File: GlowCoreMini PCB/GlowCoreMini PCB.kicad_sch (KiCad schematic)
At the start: 63 parts, among them P1 Solder_Pad, P10 Solder_Pad, P11 Solder_Pad, P12 Solder_Pad, P13 Solder_Pad, P14 Solder_Pad, P2 Solder_Pad, P3 Solder_Pad, P4 Solder_Pad, P5 Solder_Pad, P6 Solder_Pad, P7 Solder_Pad, P8 Solder_Pad, P9 Solder_Pad, SW1 TS24CA, SW2 TS24CA, SW3 TS24CA, SW4 TS24CA, U1 ESP32-WROOM-32E, U11 AO3400A, U12 CP2102-GMR, U14 UMH3N, U2 SN74LVC2T45DCUR, U3 MSM261D4030H1CPM, U4 SN74LVC1G373DBVR, U5 AP40P05, U6 SPX3819M5-L-3-3_TR, U7 SS54, U8 SK9822-EC20, U9 SN74LVC1G373DBVR

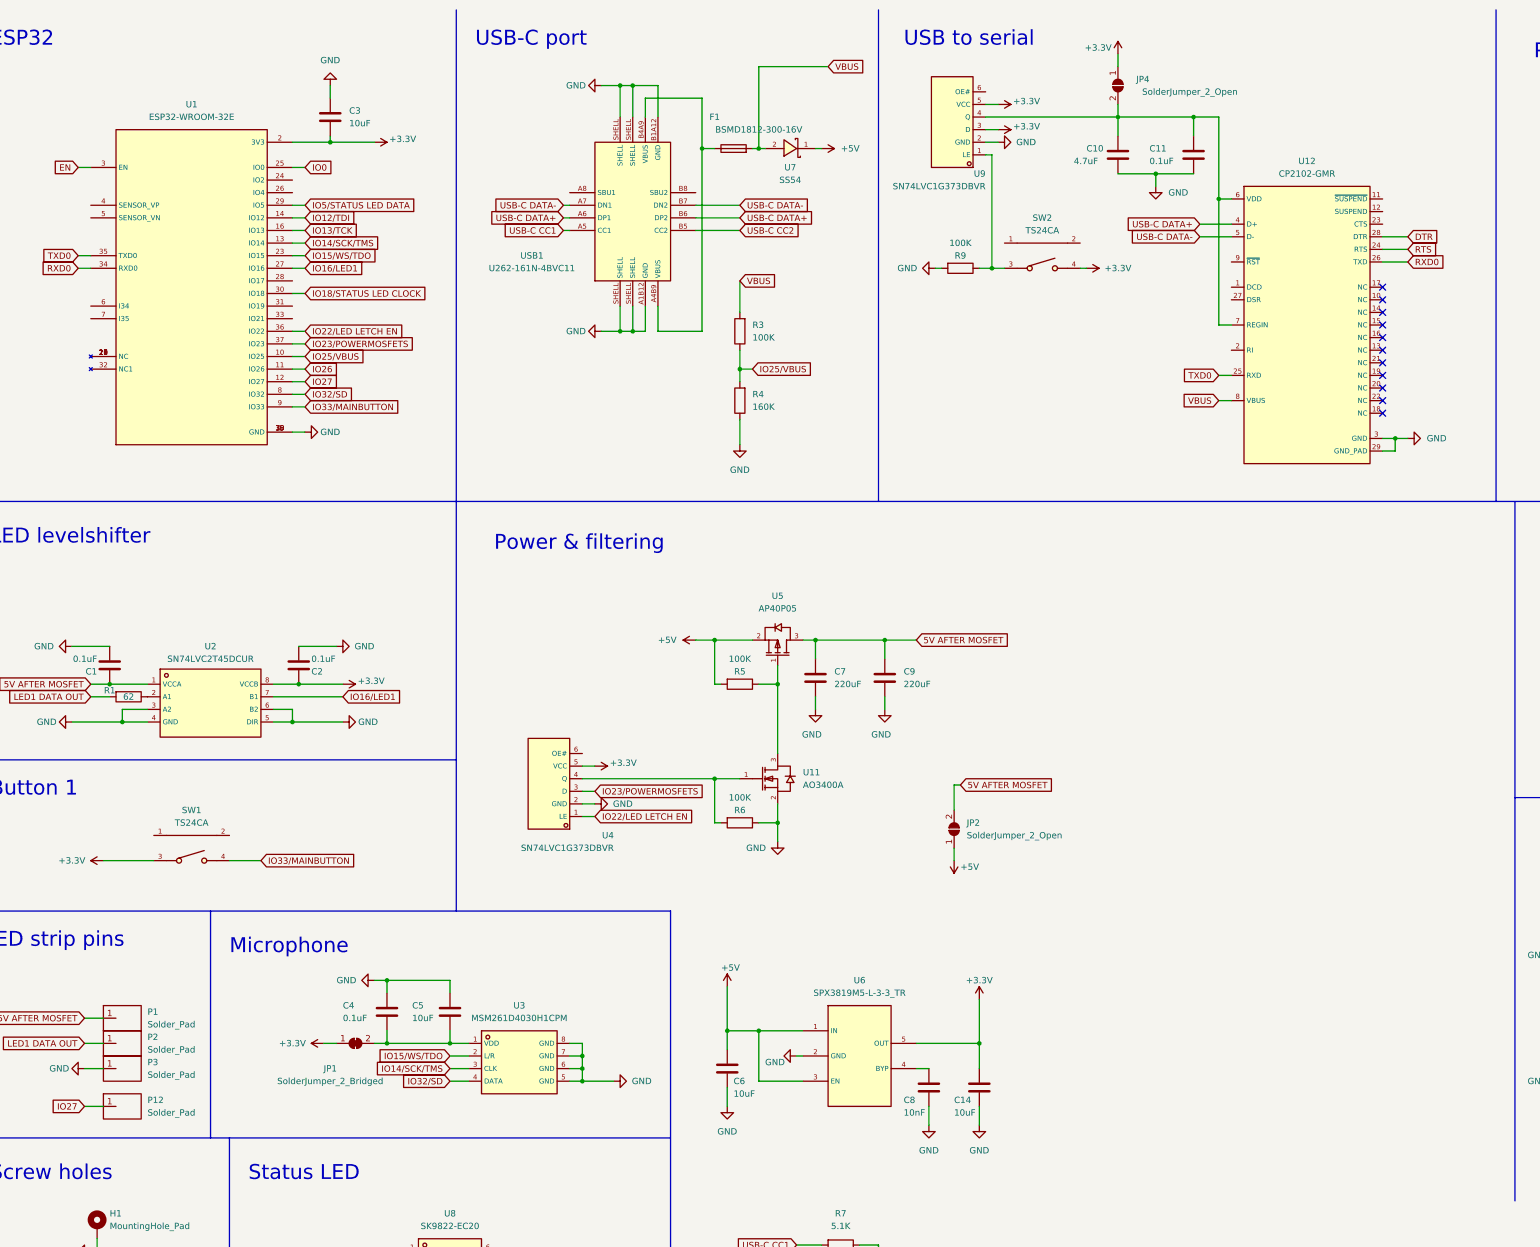
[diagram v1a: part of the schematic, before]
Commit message: updated 3D printed case design
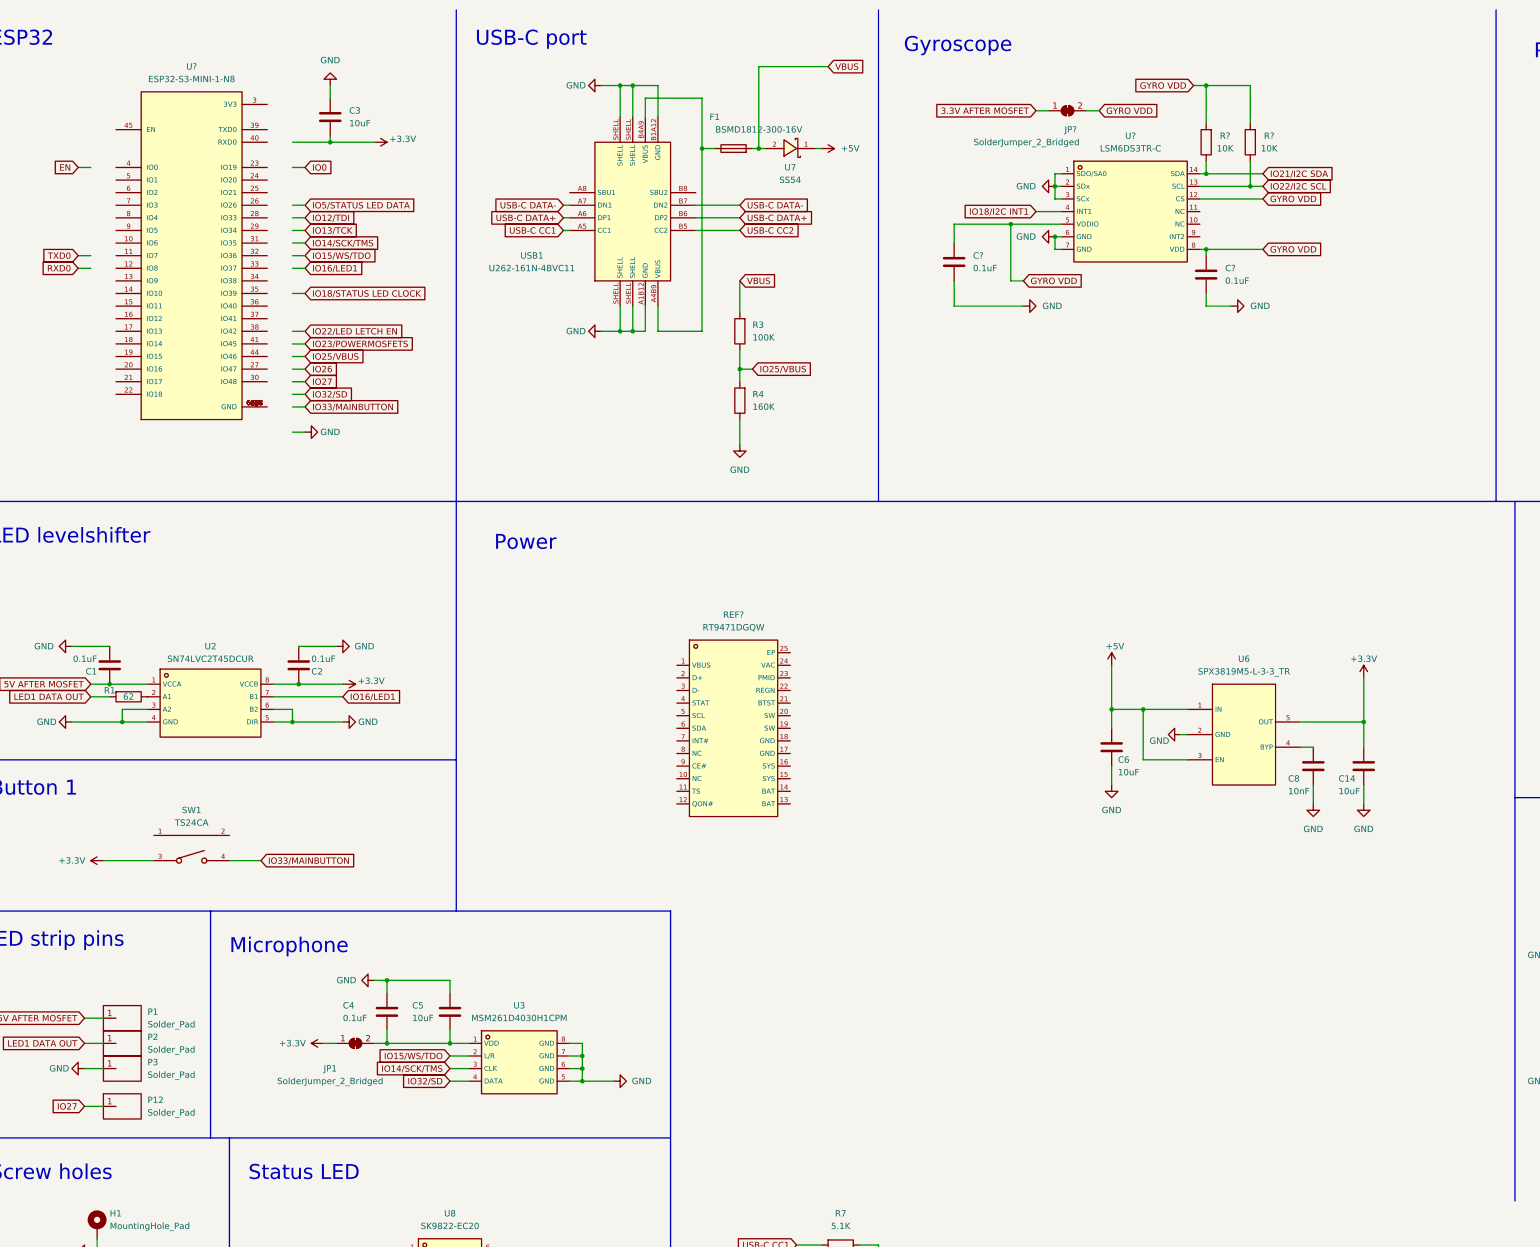
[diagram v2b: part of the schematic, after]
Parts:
- removed C10: 4.7uF, Capacitor_SMD:C_0603_1608Metric, symbol Device:C
- removed C11: 0.1uF, Capacitor_SMD:C_0402_1005Metric, symbol Device:C
- removed C7, C9: 220uF, Capacitor_SMD:C_1206_3216Metric_Pad1.33x1.80mm_HandSolder, symbol Device:C
- removed JP2, JP4: SolderJumper_2_Open, Jumper:SolderJumper-2_P1.3mm_Open_RoundedPad1.0x1.5mm, symbol Jumper:SolderJumper_2_Open
- removed R5, R6, R9: 100K, Resistor_SMD:R_0402_1005Metric, symbol Device:10K 0603
- removed SW2: TS24CA, footprint:SW-SMD_TS24CA, symbol MyParts:TS24CA
- removed U1: ESP32-WROOM-32E, footprint:WIFI-SMD_ESP32-WROOM-32E, symbol MyParts:ESP32-WROOM-32E
- removed U11: AO3400A, footprint:SOT-23-3_L2.9-W1.6-P1.90-LS2.8-BR, symbol MyParts:AO3400A
- removed U12: CP2102-GMR, footprint:QFN-28_L5.0-W5.0-P0.50-BL-EP, symbol MyParts:CP2102-GMR
- removed U4, U9: SN74LVC1G373DBVR, footprint:SOT-23-6_L2.9-W1.6-P0.95-LS2.8-BR, symbol MyParts:SN74LVC1G373DBVR
- removed U5: AP40P05, footprint:SOT-23-3_L2.9-W1.3-P1.90-LS2.4-BR, symbol MyParts:AP40P05
- added C? (x2): 0.1uF, Capacitor_SMD:C_0402_1005Metric, symbol Device:C
- added JP?: SolderJumper_2_Bridged, Jumper:SolderJumper-2_P1.3mm_Bridged_RoundedPad1.0x1.5mm, symbol Jumper:SolderJumper_2_Bridged
- added R? (x2): 10K, Resistor_SMD:R_0402_1005Metric, symbol Device:10K 0603
- added REF?: RT9471DGQW, footprint:WQFN-24_L4.0-W4.0-P0.50-TL-EP2.5, symbol MyParts:RT9471DGQW
- added U?: ESP32-S3-MINI-1-N8, footprint:ESP32-S3-MINI-1-N8, symbol MyParts:ESP32-S3-MINI-1-N8
- added U?: LSM6DS3TR-C, footprint:LGA-14_L3.0-W2.5-P0.50-TL, symbol MyParts:LSM6DS3TR-C
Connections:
- net GND: now also C?.2, C?.2, U?.1 (SDO/SA0), U?.2 (SDx), U?.3 (SCx), U?.6 (GND), U?.7 (GND)
- new net: U?.1 (GND), U?.2 (GND), U?.42 (GND), U?.43 (GND), U?.46 (GND), U?.47 (GND), U?.48 (GND), U?.49 (GND), U?.50 (GND), U?.51 (GND), U?.52 (GND), U?.53 (GND), U?.54 (GND), U?.55 (GND), U?.56 (GND), U?.57 (GND), U?.58 (GND), U?.59 (GND), U?.60 (GND), U?.61 (GND), U?.61_1 (GND), U?.61_2 (GND), U?.61_3 (GND), U?.61_4 (GND), U?.61_5 (GND), U?.61_6 (GND), U?.61_7 (GND), U?.61_8 (GND), U?.62 (GND), U?.63 (GND), U?.64 (GND), U?.65 (GND)
- new net 3.3V AFTER MOSFET: JP?.1 (A)
- new net GYRO VDD: C?.1, C?.1, JP?.2 (B), R?.2, R?.2, U?.12 (CS), U?.5 (VDDIO), U?.8 (VDD)
- new net IO18/I2C INT1: U?.4 (INT1)
- new net IO21/I2C SDA: R?.1, U?.14 (SDA)
- new net IO22/I2C SCL: R?.1, U?.13 (SCL)
- no-connect marks 11 -> 0
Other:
- note added: "Gyroscope"
- note added: "Power"
- note removed: "Power & filtering"
- note removed: "USB to serial"
- moved on the sheet: C14, C6, C8, U6

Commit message: continued redesign of pcb
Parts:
- removed C1, C2, C4, C? (x2): 0.1uF, Capacitor_SMD:C_0402_1005Metric, symbol Device:C
- removed C12, C14, C3, C6: 10uF, Capacitor_SMD:C_0603_1608Metric, symbol Device:10uF 0603
- removed C13: 1uF, Capacitor_SMD:C_0402_1005Metric, symbol Device:10uF 0603
- removed C5: 10uF, Capacitor_SMD:C_0603_1608Metric, symbol Device:0.1uF 0603
- removed C8: 10nF, Capacitor_SMD:C_0402_1005Metric, symbol Device:10uF 0603
- removed F1: BSMD1812-300-16V, Fuse:Fuse_1812_4532Metric_Pad1.30x3.40mm_HandSolder, symbol Device:Fuse
- removed H1, H2: MountingHole_Pad, MountingHole:MountingHole_2.2mm_M2_ISO7380, symbol Mechanical:MountingHole_Pad
- removed JP1, JP?: SolderJumper_2_Bridged, Jumper:SolderJumper-2_P1.3mm_Bridged_RoundedPad1.0x1.5mm, symbol Jumper:SolderJumper_2_Bridged
- removed P1, P10, P11, P12, P13, P14, P2, P3, P4, P5, P6, P7, P8, P9: Solder_Pad, footprint:Solder pad, symbol MyParts:Solder_Pad
- removed R1: 62, Resistor_SMD:R_0402_1005Metric, symbol Device:R
- removed R12, R13: 220, Resistor_SMD:R_0402_1005Metric, symbol Device:10K 0603
- removed R14, R15, R? (x2): 10K, Resistor_SMD:R_0402_1005Metric, symbol Device:10K 0603
- removed R3: 100K, Resistor_SMD:R_0402_1005Metric, symbol Device:R
- removed R4: 160K, Resistor_SMD:R_0603_1608Metric, symbol Device:R
- removed R7, R8: 5.1K, Resistor_SMD:R_0402_1005Metric, symbol Device:5.1K 1% 0603
- removed REF?: RT9471DGQW, footprint:WQFN-24_L4.0-W4.0-P0.50-TL-EP2.5, symbol MyParts:RT9471DGQW
- removed SW1, SW3, SW4: TS24CA, footprint:SW-SMD_TS24CA, symbol MyParts:TS24CA
- removed U14: UMH3N, footprint:SC-70-6_L2.2-W1.3-P0.65-LS2.1-BR, symbol LCSC:UMH3N
- removed U2: SN74LVC2T45DCUR, footprint:VSSOP-8_L2.4-W2.1-P0.50-LS3.2-BR, symbol MyParts:SN74LVC2T45DCUR
- removed U3: MSM261D4030H1CPM, footprint:MIC-SMD_8P-L3.0-W4.0-P0.85-BL, symbol MyParts:MSM261D4030H1CPM
- removed U6: SPX3819M5-L-3-3_TR, footprint:SOT-23-5_L3.0-W1.7-P0.95-LS2.8-BR, symbol MyParts:SPX3819M5-L-3-3_TR
- removed U7: SS54, footprint:SMA_L4.4-W2.8-LS5.4-RD, symbol MyParts:SS54
- removed U8: SK9822-EC20, footprint:LED-SMD_6P-L2.0-W2.0-P0.80-TL, symbol MyParts:SK9822-EC20
- removed U?: ESP32-S3-MINI-1-N8, footprint:ESP32-S3-MINI-1-N8, symbol MyParts:ESP32-S3-MINI-1-N8
- removed U?: LSM6DS3TR-C, footprint:LGA-14_L3.0-W2.5-P0.50-TL, symbol MyParts:LSM6DS3TR-C
- removed USB1: U262-161N-4BVC11, footprint:USB-3.1-SMD_U262-161N-4BVC11, symbol MyParts:U262-161N-4BVC11
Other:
- added sheet 3.3V converter (3_3_converter.kicad_sch)
- added sheet Battery (battery.kicad_sch)
- added sheet Battery Management IC (GlowCoreMini_BattIC.kicad_sch)
- added sheet Buttons (buttons.kicad_sch)
- added sheet ESP32 (GlowCoreMini_ESP32.kicad_sch)
- added sheet Gyroscope (gyroscope.kicad_sch)
- added sheet LED power (GlowCoreMini_LEDpower.kicad_sch)
- added sheet LED strips (ledstrips.kicad_sch)
- added sheet Microphone (microphone.kicad_sch)
- added sheet Pads (pads.kicad_sch)
- added sheet Status LED (statusled.kicad_sch)
- added sheet USB-C (GlowCoreMini_USBC.kicad_sch)
- note added: "3.3V converter"
- note added: "Battery"
- note added: "Battery IC"
- note added: "Buttons"
- note added: "GlowCore Mini"
- note added: "LED Power"
- note added: "LED strips"
- note added: "USB-C"
- note added: "v3.1"
- note removed: "Auto program DTR RTS --> EN IO0 1 1 1 1 0 0 1 1 1 0 0 1 0 1 1 0"
- note removed: "Autoreset"
- note removed: "Button 1"
- note removed: "LED levelshifter"
- note removed: "LED strip pins"
- note removed: "Power"
- note removed: "Reset"
- note removed: "Screw holes"
- note removed: "USB-C port"

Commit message: updated pcb design
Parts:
- added C1, C12: 1uF, Capacitor_SMD:C_0402_1005Metric, symbol Device:10uF 0603
- added C10, C11, C14, C16: 0.1uF, Capacitor_SMD:C_0402_1005Metric, symbol Device:C
- added C13: 0.1uF, Capacitor_SMD:C_0402_1005Metric, symbol Device:0.1uF 0603
- added C15: 10uF, Capacitor_SMD:C_0603_1608Metric, symbol Device:0.1uF 0603
- added C17, C19, C2, C3, C7, C8, C9: 10uF, Capacitor_SMD:C_0603_1608Metric, symbol Device:10uF 0603
- added C18: 10nF, Capacitor_SMD:C_0402_1005Metric, symbol Device:10uF 0603
- added C4: 220uF, Capacitor_SMD:C_1206_3216Metric, symbol Device:C
- added C5: 4.7uF, Capacitor_SMD:C_0402_1005Metric, symbol Device:10uF 0603
- added C6: 47nF, Capacitor_SMD:C_0402_1005Metric, symbol Device:10uF 0603
- added F1: BSMD1812-300-16V, Fuse:Fuse_1812_4532Metric_Pad1.30x3.40mm_HandSolder, symbol Device:Fuse
- added JP1: SolderJumper_2_Open, Jumper:SolderJumper-2_P1.3mm_Open_RoundedPad1.0x1.5mm, symbol Jumper:SolderJumper_2_Open
- added JP2: SolderJumper_2_Bridged, Jumper:SolderJumper-2_P1.3mm_Bridged_RoundedPad1.0x1.5mm, symbol Jumper:SolderJumper_2_Bridged
- added L1: WPN4020H1R0MT, footprint:IND-SMD_L4.0-W4.0_SLW40XX, symbol MyParts:WPN4020H1R0MT
- added P1, P10, P11, P12, P13, P14, P15, P16, P17, P18, P19, P2, P20, P21, P22, P3, P4, P5, P6, P7, P8, P9: Solder_Pad, footprint:Solder pad, symbol MyParts:Solder_Pad
- added R1, R13, R16, R19, R3, R9: 100K, Resistor_SMD:R_0402_1005Metric, symbol Device:R
- added R10, R11, R2, R20, R7, R8: 10K, Resistor_SMD:R_0402_1005Metric, symbol Device:10K 0603
- added R12, R21, R22, R5, R6: 100K, Resistor_SMD:R_0402_1005Metric, symbol Device:10K 0603
- added R14, R15: 62, Resistor_SMD:R_0402_1005Metric, symbol Device:R
- added R17, R23, R24: 5.1K, Resistor_SMD:R_0402_1005Metric, symbol Device:5.1K 1% 0603
- added R18: 33K, Resistor_SMD:R_0402_1005Metric, symbol Device:R
- added R4: 160K, Resistor_SMD:R_0603_1608Metric, symbol Device:R
- added REF1: RT9471DGQW, footprint:RT9471_vias_in_pad, symbol MyParts:RT9471DGQW
- added SW1, SW2, SW3: TS24CA, footprint:SW-SMD_TS24CA, symbol MyParts:TS24CA
- added U1: SN74LVC1G373DBVR, footprint:SOT-23-6_L2.9-W1.6-P0.95-LS2.8-BR, symbol MyParts:SN74LVC1G373DBVR
- added U10: LSM6DS3TR-C, footprint:LGA-14_L3.0-W2.5-P0.50-TL, symbol MyParts:LSM6DS3TR-C
- added U11: MSM261D4030H1CPM, footprint:MIC-SMD_8P-L4.0-W3.0_ZTS6231, symbol MyParts:MSM261D4030H1CPM
- added U12: SPX3819M5-L-3-3_TR, footprint:SOT-23-5_L3.0-W1.7-P0.95-LS2.8-BR, symbol MyParts:SPX3819M5-L-3-3_TR
- added U13: SK9822-EC20, footprint:LED-SMD_6P-L2.0-W2.0-P0.80-TL, symbol MyParts:SK9822-EC20
- added U14, U15, U4, U5, U8: AP40P05, footprint:SOT-23-3_L2.9-W1.3-P1.90-LS2.4-BR, symbol MyParts:AP40P05
- added U2: ESP32-S3-MINI-1-N8, footprint:ESP32-S3-MINI-1-N8, symbol MyParts:ESP32-S3-MINI-1-N8
- added U3: PTVSHC3N12VU, footprint:DFN-3_L2.0-W2.0-P1.30-BR, symbol MyParts:PTVSHC3N12VU
- added U6: AO3400A, footprint:SOT-23-3_L2.9-W1.6-P1.90-LS2.8-BR, symbol MyParts:AO3400A
- added U7: 74LVC2G04DW-7, footprint:SOT-363_L2.0-W1.3-P0.65-LS2.1-BR, symbol MyParts:74LVC2G04DW-7
- added U9: SN74LVC2T45DCUR, footprint:VSSOP-8_L2.4-W2.1-P0.50-LS3.2-BR, symbol MyParts:SN74LVC2T45DCUR
- added USB1: U262-161N-4BVC11, footprint:USB-3.1-SMD_U262-161N-4BVC11, symbol MyParts:U262-161N-4BVC11
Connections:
- new net: R15.1, U9.3 (A2)
- new net: C6.1, REF1.21 (BTST)
- new net: C6.2, L1.1, REF1.19 (SW), REF1.20 (SW)
- new net: R12.1, R21.1, R22.2, R5.1, U14.1 (G), U15.1 (G), U4.1 (G), U5.1 (G), U6.3 (D)
- new net: R10.2, R11.2, REF1.11 (TS)
- new net: C8.2, C9.2, JP2.1 (A), L1.2, REF1.15 (SYS), REF1.16 (SYS)
- new net: C2.2, REF1.23 (PMID)
- new net: P1.1, U8.3 (D)
- new net: C18.2, U12.4 (BYP)
- new net: R14.1, U9.2 (A1)
- new net: R6.2, U1.4 (Q), U6.1 (G)
- new net: R9.1, SW1.4, U7.1 (1A)
- new net: F1.1, JP1.1 (A), USB1.A4B9 (VBUS), USB1.B4A9 (VBUS)
- new net: R13.2, U8.1 (G)
- new net +3V3: C19.2, C3.2, P20.1, R12.2, R16.1, R17.1, R2.1, R20.1, R7.1, R8.1, R9.2, U1.5 (VCC), U12.5 (OUT), U15.2 (S), U2.3 (3V3), U7.5 (VCC)
- new net +BATT: C7.2, R18.2, REF1.13 (BAT), REF1.14 (BAT), U8.2 (S)
- new net -BATT: C1.1, C10.2, C11.2, C12.1, C13.1, C14.2, C15.1, C16.2, C17.1, C18.1, C19.1, C2.1, C3.1, C4.2, C5.2, C7.1, C8.1, C9.1, P15.1, P18.1, P2.1, P5.1, R1.2, R11.1, R13.1, R19.1, R23.1, R24.1, R4.1, R6.1, REF1.17 (GND), REF1.18 (GND), REF1.25 (EP), SW1.3, SW2.3, SW3.3, U1.2 (GND), U10.1 (SDO/SA0), U10.2 (SDx), U10.3 (SCx), U10.6 (GND), U10.7 (GND), U11.5 (GND), U11.6 (GND), U11.7 (GND), U11.8 (GND), U12.2 (GND), U13.2 (GND), U2.1 (GND), U2.2 (GND), U2.42 (GND), U2.43 (GND), U2.46 (GND), U2.47 (GND), U2.48 (GND), U2.49 (GND), U2.50 (GND), U2.51 (GND), U2.52 (GND), U2.53 (GND), U2.54 (GND), U2.55 (GND), U2.56 (GND), U2.57 (GND), U2.58 (GND), U2.59 (GND), U2.60 (GND), U2.61 (GND), U2.61_1 (GND), U2.61_2 (GND), U2.61_3 (GND), U2.61_4 (GND), U2.61_5 (GND), U2.61_6 (GND), U2.61_7 (GND), U2.61_8 (GND), U2.62 (GND), U2.63 (GND), U2.64 (GND), U2.65 (GND), U3.1 (A), U3.2 (1), U6.2 (S), U7.2 (GND), U9.4 (GND), U9.5 (DIR), USB1.A1B12 (GND), USB1.B1A12 (GND), USB1.SHELL
- new net 3.3V AFTER MOSFET: C11.1, C13.2, C14.1, C15.2, C16.1, P10.1, U10.12 (CS), U10.5 (VDDIO), U10.8 (VDD), U11.1 (VDD), U15.3 (D), U9.8 (VCCB)
- new net 5V AFTER MOSFET: C10.1, P16.1, P3.1, U13.5 (VDD), U14.3 (D), U4.3 (D), U5.3 (D), U9.1 (VCCA)
- new net EN: C12.2, P11.1, R17.2, SW3.4, U2.45 (EN)
- new net IO0/BOOT: R16.2, SW2.4, U2.4 (IO0), U7.3 (2A)
- new net IO10/I2C GRYO INT: R8.2, U10.4 (INT1), U2.14 (IO10)
- new net IO11/I2C BATT IC INT: R20.2, REF1.7 (INT#), U2.15 (IO11)
- new net IO12/I2S WS: U11.2 (L/R), U2.16 (IO12)
- new net IO13/I2S SCK: U11.3 (CLK), U2.17 (IO13)
- new net IO14/I2S SD: U11.4 (DATA), U2.18 (IO14)
- new net IO15/LED LETCH EN: U1.1 (LE), U2.19 (IO15)
- new net IO16/POWERMOSFETS: U1.3 (D), U2.20 (IO16)
- new net IO1/POWERBUTTON: P13.1, U2.5 (IO1), U7.6 (1Y)
- new net IO2/BATT VOLT: R18.1, R19.2, U2.6 (IO2)
- new net IO35/SPI MO: P7.1, U2.31 (IO35)
- new net IO36/SPI SCK: P6.1, U2.32 (IO36)
- new net IO37/SPI MI: P19.1, U2.33 (IO37)
- new net IO39/STATUS LED CLOCK: U13.4 (CKL), U2.35 (IO39)
- new net IO3/ACTIONBUTTON: P14.1, U2.7 (IO3), U7.4 (2Y)
- new net IO40/STATUS LED DATA: U13.3 (SDI), U2.36 (IO40)
- new net IO41/LED1: U2.37 (IO41), U9.7 (B1)
- new net IO42/LED2: U2.38 (IO42), U9.6 (B2)
- new net IO47/BATT IC EN: R1.1, REF1.9 (CE#), U2.27 (IO47)
- new net IO7/VBUS: R3.1, R4.2, U2.11 (IO7)
- new net IO8/I2C SDA: P22.1, R2.2, REF1.6 (SDA), U10.14 (SDA), U2.12 (IO8)
- new net IO9/I2C SCL: P21.1, R7.2, REF1.5 (SCL), U10.13 (SCL), U2.13 (IO9)
- new net LED1 DATA OUT: P12.1, R14.2
- new net LED2 DATA OUT: P17.1, R15.2
- new net REGN: C5.1, R10.1, REF1.22 (REGN)
- new net RXD0: P9.1, U2.40 (RXD0)
- new net TXD0: P8.1, U2.39 (TXD0)
- new net USB D+: U2.24 (IO20), USB1.A6 (DP1), USB1.B6 (DP2)
- new net USB D-: U2.23 (IO19), USB1.A7 (DN1), USB1.B7 (DN2)
- new net USB-C CC1: R23.2, USB1.A5 (CC1)
- new net USB-C CC2: R24.2, USB1.B5 (CC2)
- new net VBUS: C1.2, C4.1, F1.2, P4.1, R21.2, R22.1, R3.2, R5.2, REF1.1 (VBUS), REF1.24 (VAC), U14.2 (S), U3.3 (K), U4.2 (S), U5.2 (S)
- new net VSYS: C17.2, JP1.2 (B), JP2.2 (B), U12.1 (IN), U12.3 (EN)
- no-connect marks 0 -> 33
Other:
- removed sheet 3.3V converter
- removed sheet Battery
- removed sheet Battery Management IC
- removed sheet Buttons
- removed sheet ESP32
- removed sheet Gyroscope
- removed sheet LED power
- removed sheet LED strips
- removed sheet Microphone
- removed sheet Pads
- removed sheet Status LED
- removed sheet USB-C
- note added: "+BATT"
- note added: "-BATT"
- note added: "Battery Management IC & Boost Converter"
- note added: "GlowCore Mini has the ability to completely turn of power for the connected LEDs, to reduce power consumption when the LEDs are not used. Multiple MOSFETs (U15, U14 and so on) are used for that purpose. A single WS2812B LED for example would otherwise still consume 1mA, even when off. But to also enable a power saving mode, where the ESP32 goes to sleep, while the LEDs stay on - GlowCore Mini als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"
- note added: "LED power"
- note added: "LED strip pads"
- note added: "The ESP32 is the microcontroller used in GlowCore Mini. It comes preinstalled with GlowOS, a customized fork of the open source software WLED."
- note added: "USB-C port"
- note removed: "Battery IC"
- note removed: "LED Power"
- note removed: "LED strips"
- note removed: "USB-C"
